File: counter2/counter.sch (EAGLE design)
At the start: 46 parts, among them IC1 MCP1703DB, IC2 4067D, IC3 74HC154DW, J1 RJ12RIGHTANGLE-I2C, X2 8MHz, X4 MINI-USB

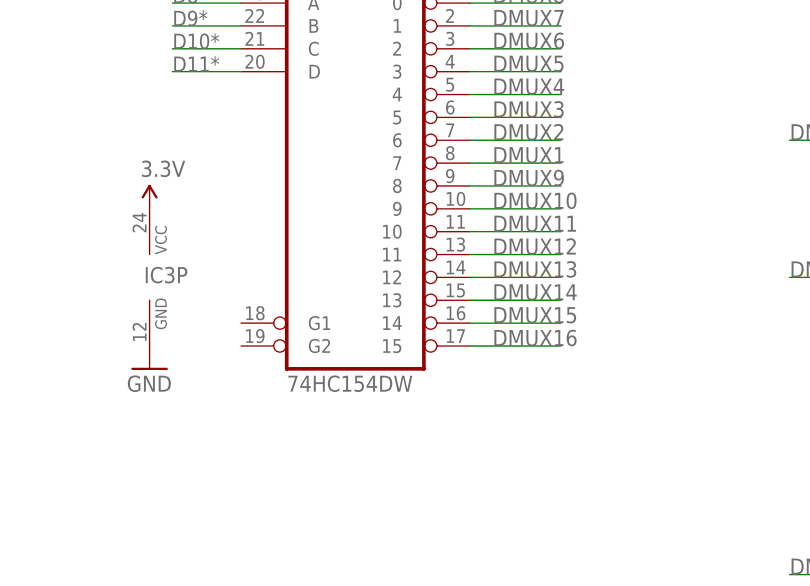
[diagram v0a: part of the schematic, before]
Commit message: set 74HC154D to gnd
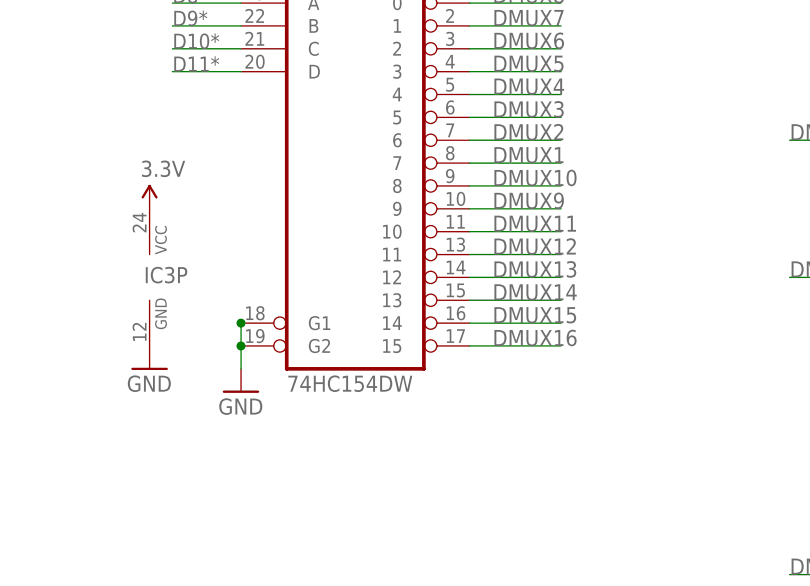
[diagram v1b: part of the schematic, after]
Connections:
- net DMUX10: now also IC3A.8; no longer IC3A.9
- net DMUX9: now also IC3A.9; no longer IC3A.8
- net GND: now also IC3A.G1, IC3A.G2
